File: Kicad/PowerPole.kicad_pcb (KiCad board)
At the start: 2 copper layers, 113 x 102.9 mm, 49 parts, among them J1 Anderson powerpole, J2 Anderson powerpole, J3 Anderson powerpole, J4 Anderson powerpole, J5 Anderson powerpole, J6 Meter +ve, J7 Meter GND, J8 Meter LOAD, K1 896HP-1AH-C-12VDC, SW1 SW_Push

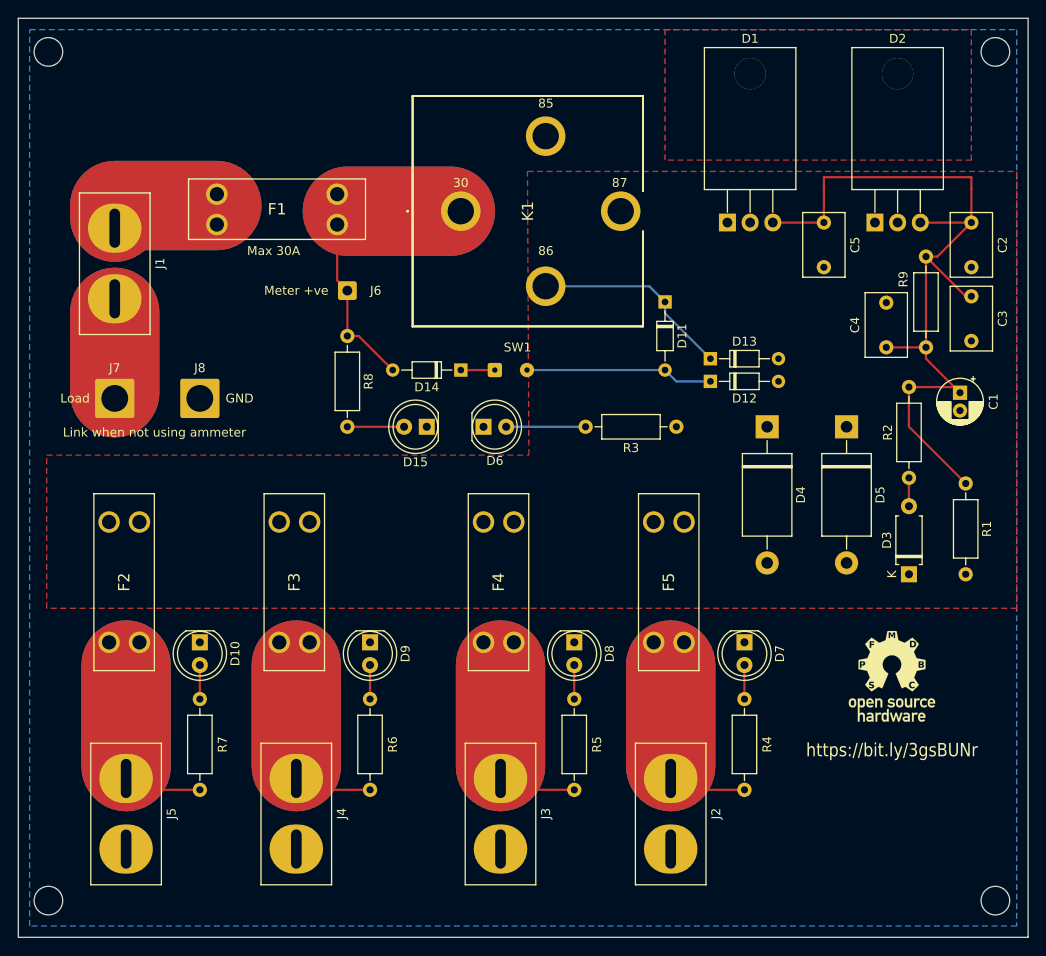
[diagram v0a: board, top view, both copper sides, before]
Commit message: Updated to v1.1. powerpole sinkscreen and sw1 pads updated
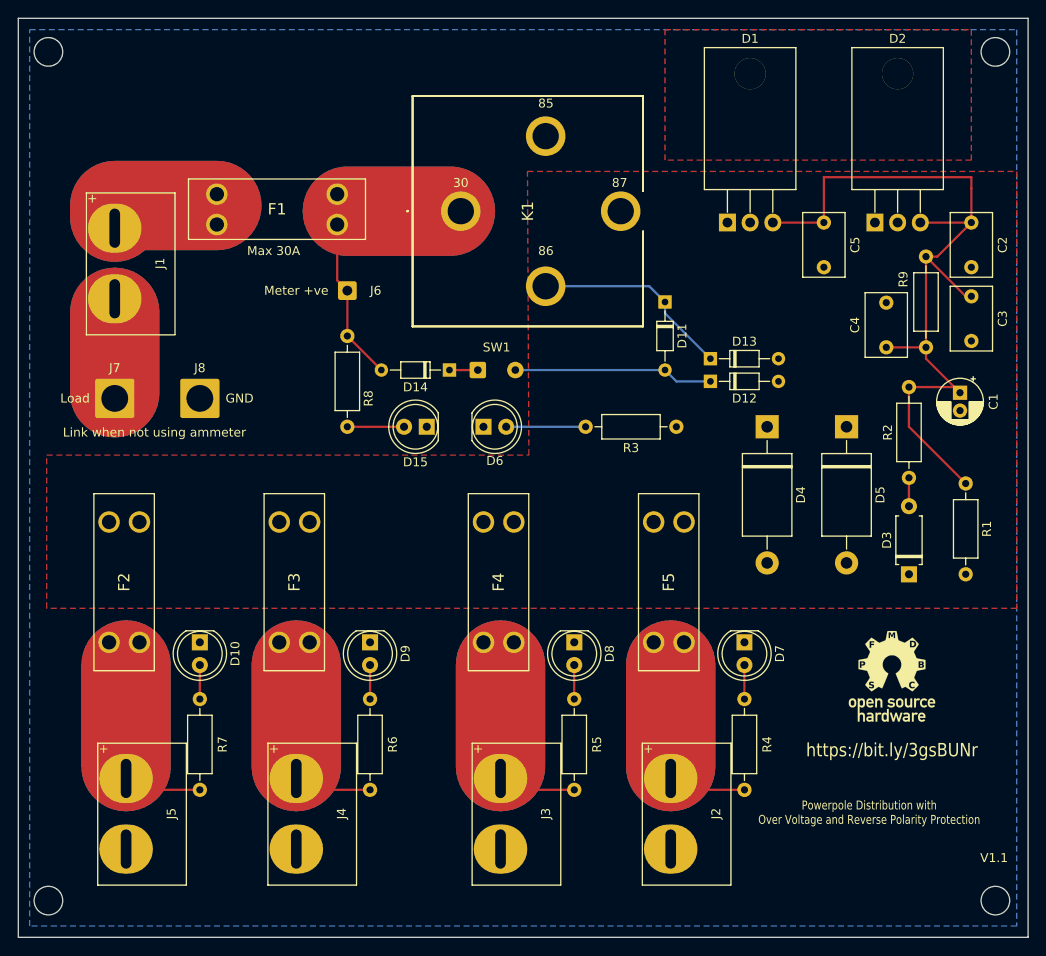
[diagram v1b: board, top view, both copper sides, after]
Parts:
- R3, R4, R5, R6, R7, R8: value 220K -> 2K2
- SW1: footprint Connector_Wire:SolderWire-0.1sqmm_1x02_P3.6mm_D0.4mm_OD1mm -> Connector_Wire:SolderWire-0.25sqmm_1x02_P4.2mm_D0.65mm_OD1.7mm
- moved SW1 1.91 mm to (139.1, 54.6)
- moved D14 1.27 mm to (135.9, 54.6)
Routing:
- net Net-(D11-Pad2): track 21.1 -> 22.4 mm
- net Net-(D14-Pad2): track 42.7 -> 41.4 mm
- net Net-(D14-Pad1): track 3.81 -> 3.18 mm
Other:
- board text added: "Powerpole Distribution with Over Voltage and Reverse Polarity Protection"
- board text added: "V1.1"
